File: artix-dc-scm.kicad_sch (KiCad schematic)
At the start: 2 parts

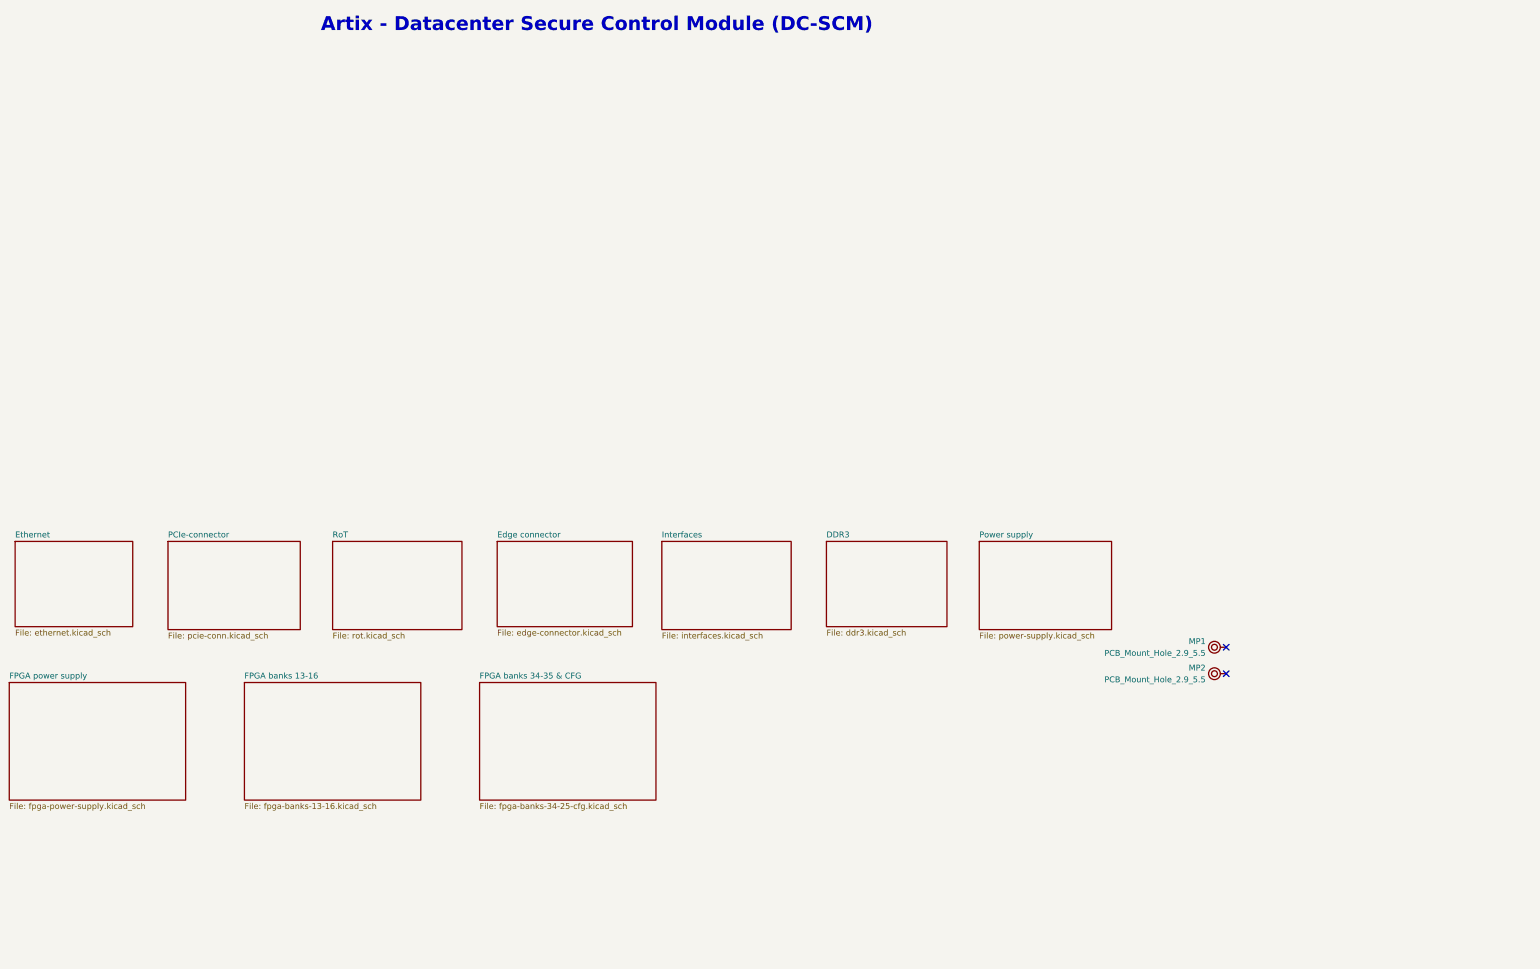
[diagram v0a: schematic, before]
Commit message: [#55652] Fix hotareas
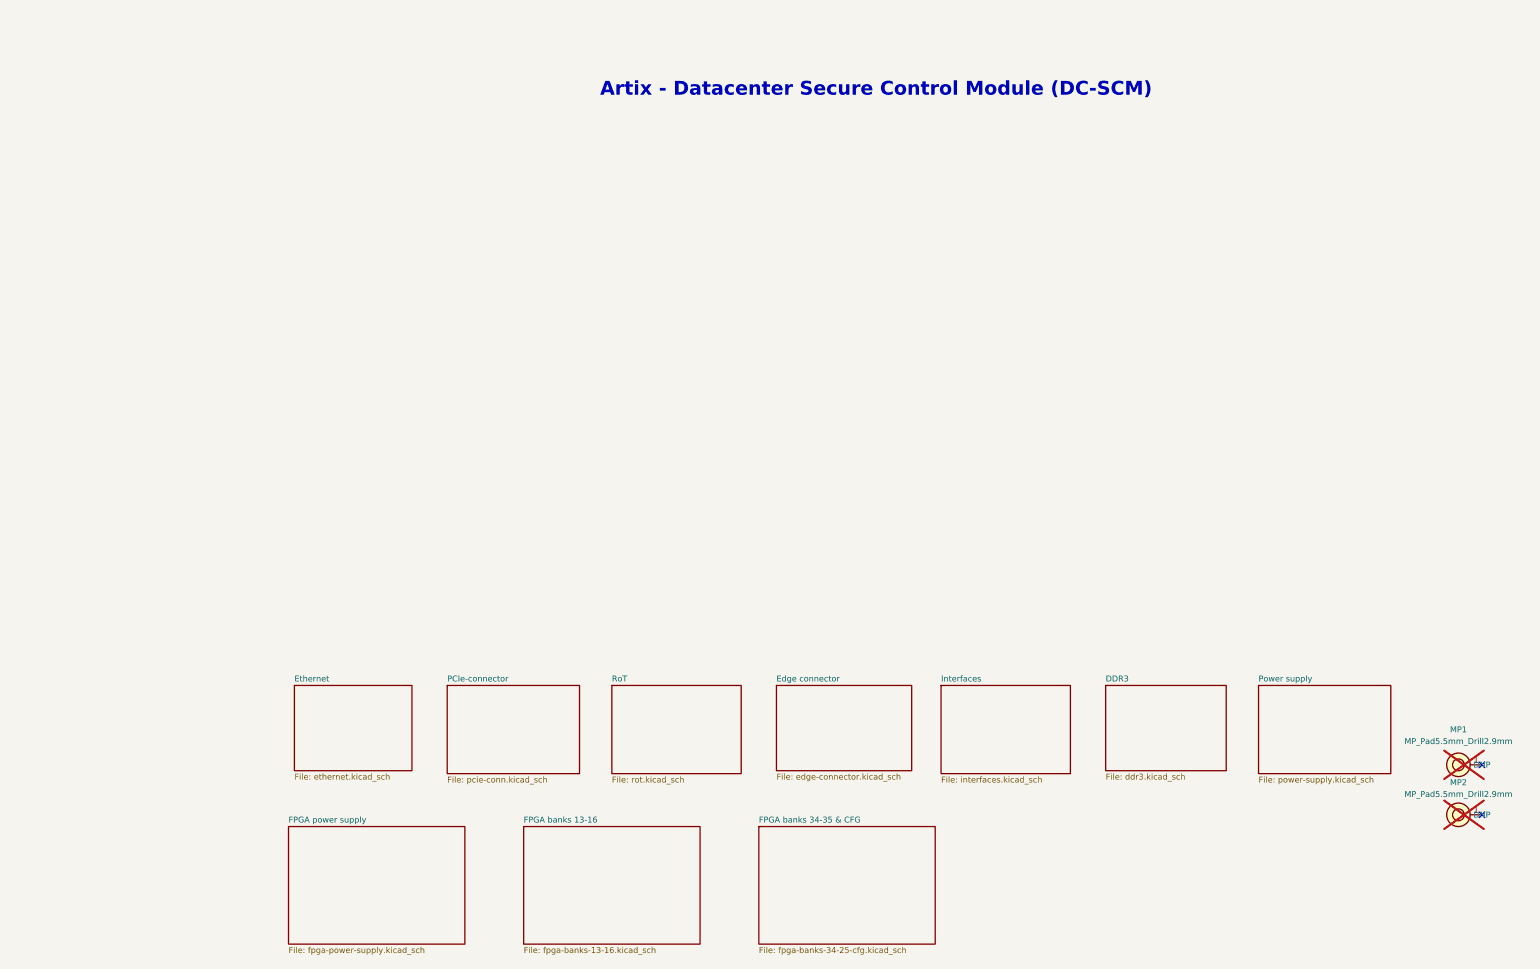
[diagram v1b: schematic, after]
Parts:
- MP1, MP2: value PCB_Mount_Hole_2.9_5.5 -> MP_Pad5.5mm_Drill2.9mm; footprint antmicro-footprints:mounting-hole-2.9mm-5.5mm -> antmicro-footprints:MP_Pad5.5mm_Drill2.9mm; symbol antmicroMechanicalParts:PCB_Mount_Hole_2.9_5.5 -> antmicroMechanicalParts:MP_Pad5.5mm_Drill2.9mm; now not fitted; now left out of the parts list

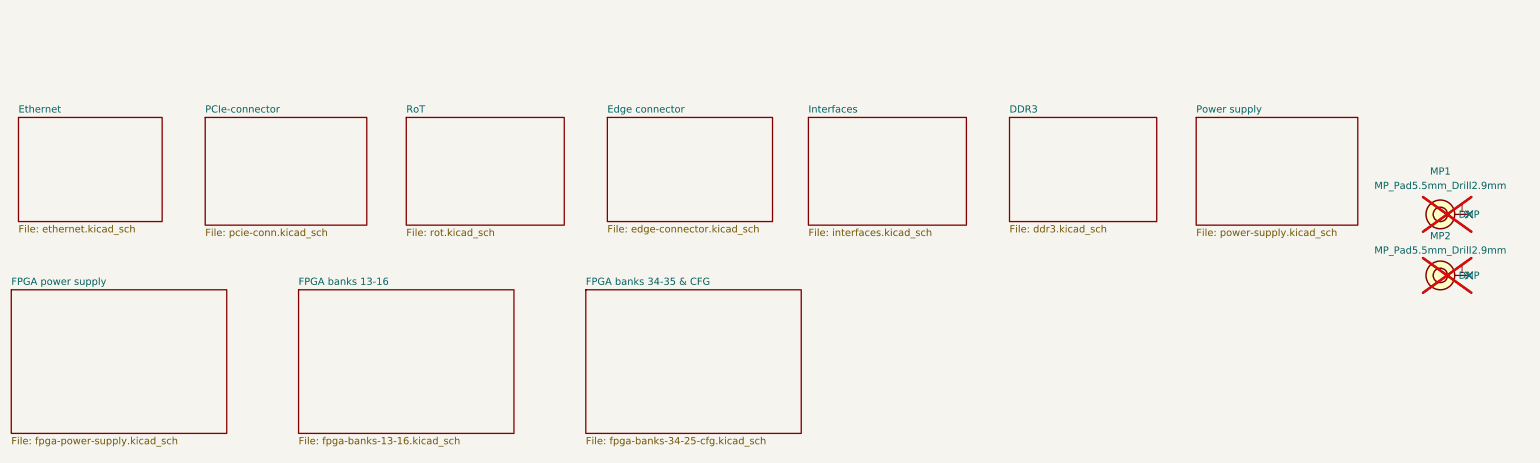
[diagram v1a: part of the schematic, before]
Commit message: [#68236] Allign sch to grid
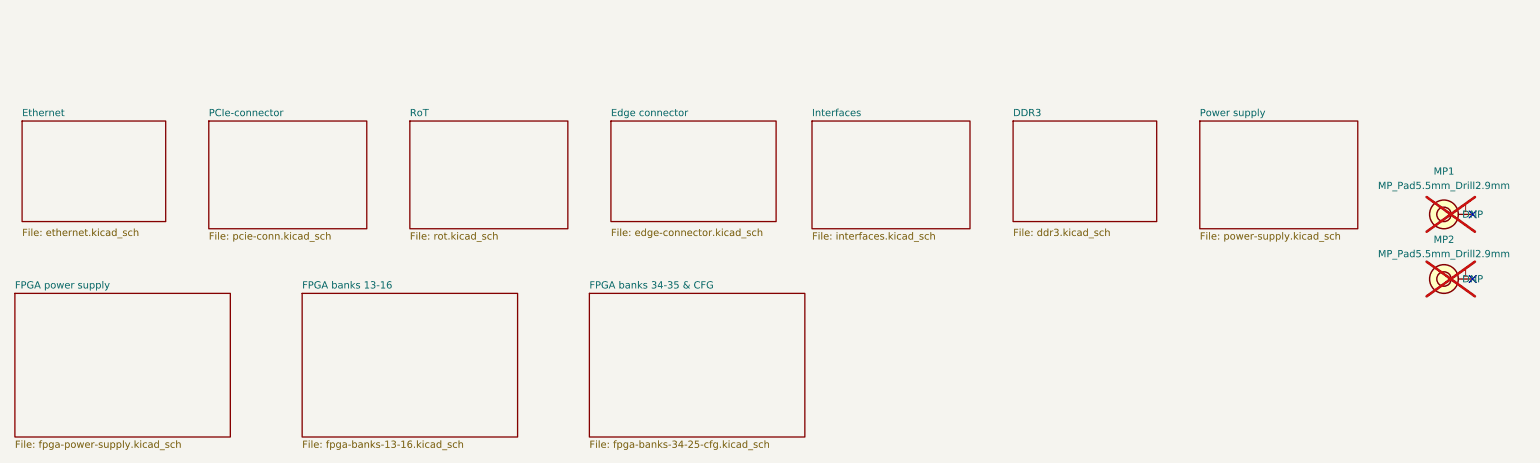
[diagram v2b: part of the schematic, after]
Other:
- moved on the sheet: MP1, MP2

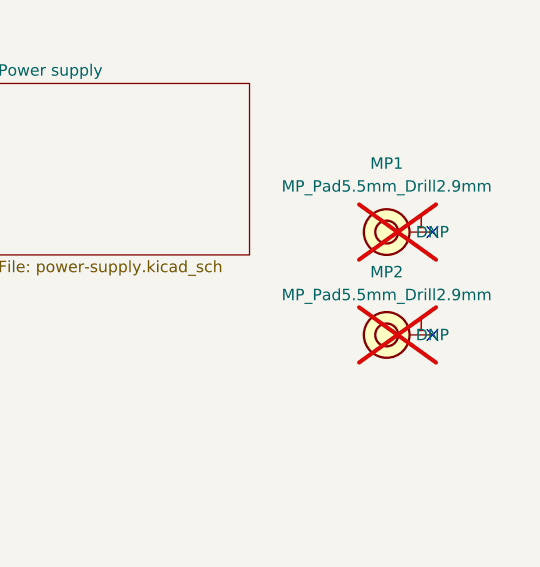
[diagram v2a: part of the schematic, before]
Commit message: [#68236] Remove DNP property from Testpoints
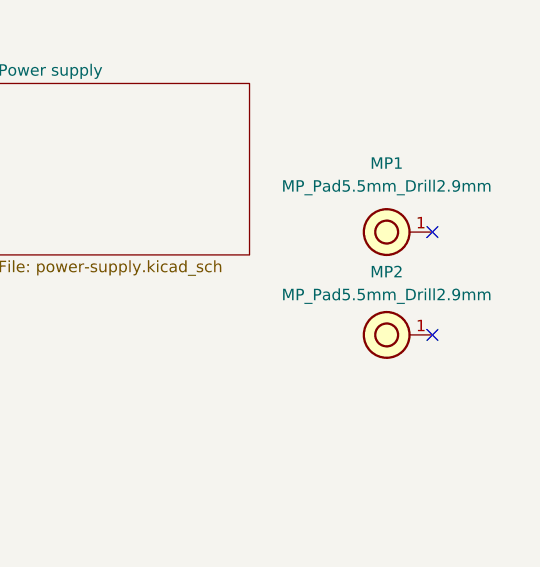
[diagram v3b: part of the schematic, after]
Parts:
- MP1, MP2: DNP DNP -> (none); now fitted
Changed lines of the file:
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@@
   )
   (symbol (lib_id "antmicroMechanicalParts:MP_Pad5.5mm_Drill2.9mm") (at 337.82 182.88 0) (mirror y) (unit 1)
-    (in_bom no) (on_board yes) (dnp yes) (fields_autoplaced)
+    (in_bom no) (on_board yes) (dnp no) (fields_autoplaced)
     (property "Reference" "MP1" (at 332.74 175.26 0)
       (effects (font (size 1.27 1.27)))
@@
       (effects (font (size 1.27 1.27) (thickness 0.15)) (justify left bottom) hide)
     )
-    (property "DNP" "DNP" (at 337.82 182.88 0)
-      (effects (font (size 1.27 1.27)))
-    )
     (pin "1")
     (instances
@@
   )
   (symbol (lib_id "antmicroMechanicalParts:MP_Pad5.5mm_Drill2.9mm") (at 337.82 194.31 0) (mirror y) (unit 1)
-    (in_bom no) (on_board yes) (dnp yes) (fields_autoplaced)
+    (in_bom no) (on_board yes) (dnp no) (fields_autoplaced)
     (property "Reference" "MP2" (at 332.74 187.325 0)
       (effects (font (size 1.27 1.27)))
@@
       (effects (font (size 1.27 1.27) (thickness 0.15)) (justify left bottom) hide)
     )
-    (property "DNP" "DNP" (at 337.82 194.31 0)
-      (effects (font (size 1.27 1.27)))
-    )
     (pin "1")
